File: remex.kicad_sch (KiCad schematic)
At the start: 8 parts

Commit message: added ADC circuits
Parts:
- added D? (x3): D_Zener, symbol Device:D_Zener
- added J?: ADC_B, symbol Connector:Screw_Terminal_01x03
- added J?: ADC_A, symbol Connector:Screw_Terminal_01x03
- added J? (x2): QEI, symbol Connector:Screw_Terminal_01x04
- added J?: ADC_C, symbol Connector:Screw_Terminal_01x03
- added R? (x6): R, symbol Device:R
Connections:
- net GND: now also D?.2 (A), D?.2 (A), D?.2 (A), J?.3 (Pin_3), J?.3 (Pin_3), J?.3 (Pin_3), R?.2, R?.2, R?.2
- net QEI circuit/GND: now also J?.1 (Pin_1)
- net QEI circuit/QEI_A_IN: now also J?.2 (Pin_2)
- net QEI circuit/QEI_B_IN: now also J?.3 (Pin_3)
- net QEI circuit/VBus: now also J?.4 (Pin_4)
- net QEI circuit1/GND: now also J?.1 (Pin_1)
- net QEI circuit1/QEI_A_IN: now also J?.2 (Pin_2)
- net QEI circuit1/QEI_B_IN: now also J?.3 (Pin_3)
- net QEI circuit1/VBus: now also J?.4 (Pin_4)
- net at U?.2 (P1.1): now also D?.1 (K), R?.1, R?.2
- net at U?.3 (P1.0): now also D?.1 (K), R?.1, R?.2
- net at U?.40 (P5.3): now also D?.1 (K), R?.1, R?.2
- new net: J?.1 (Pin_1), R?.1 (x3)

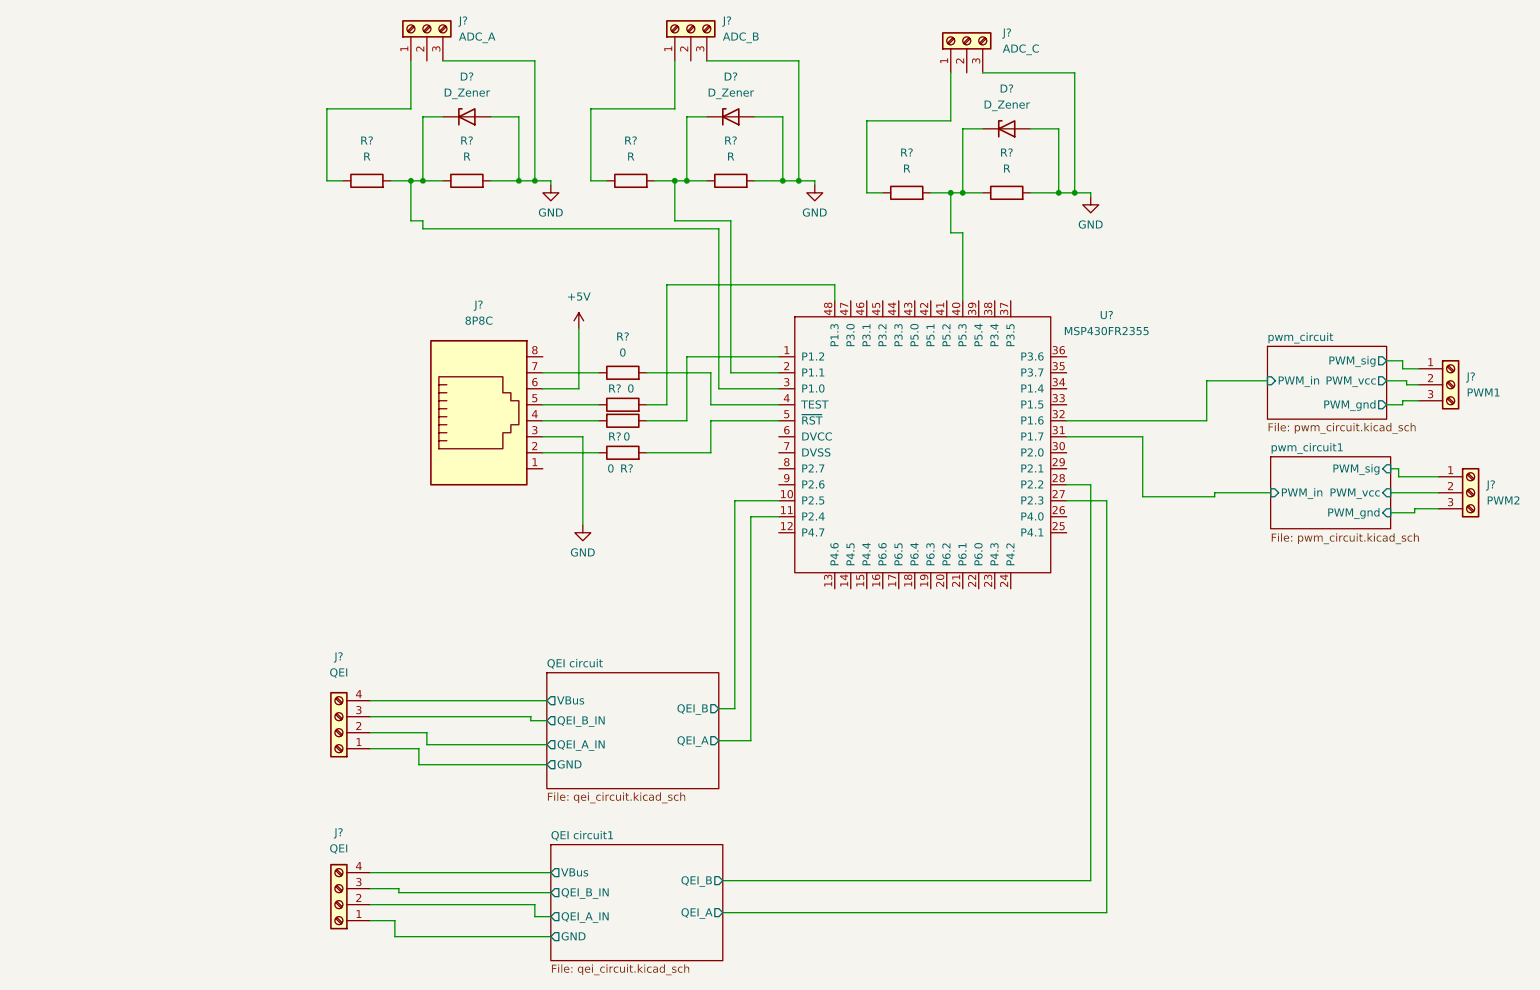
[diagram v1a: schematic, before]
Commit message: added foot prints
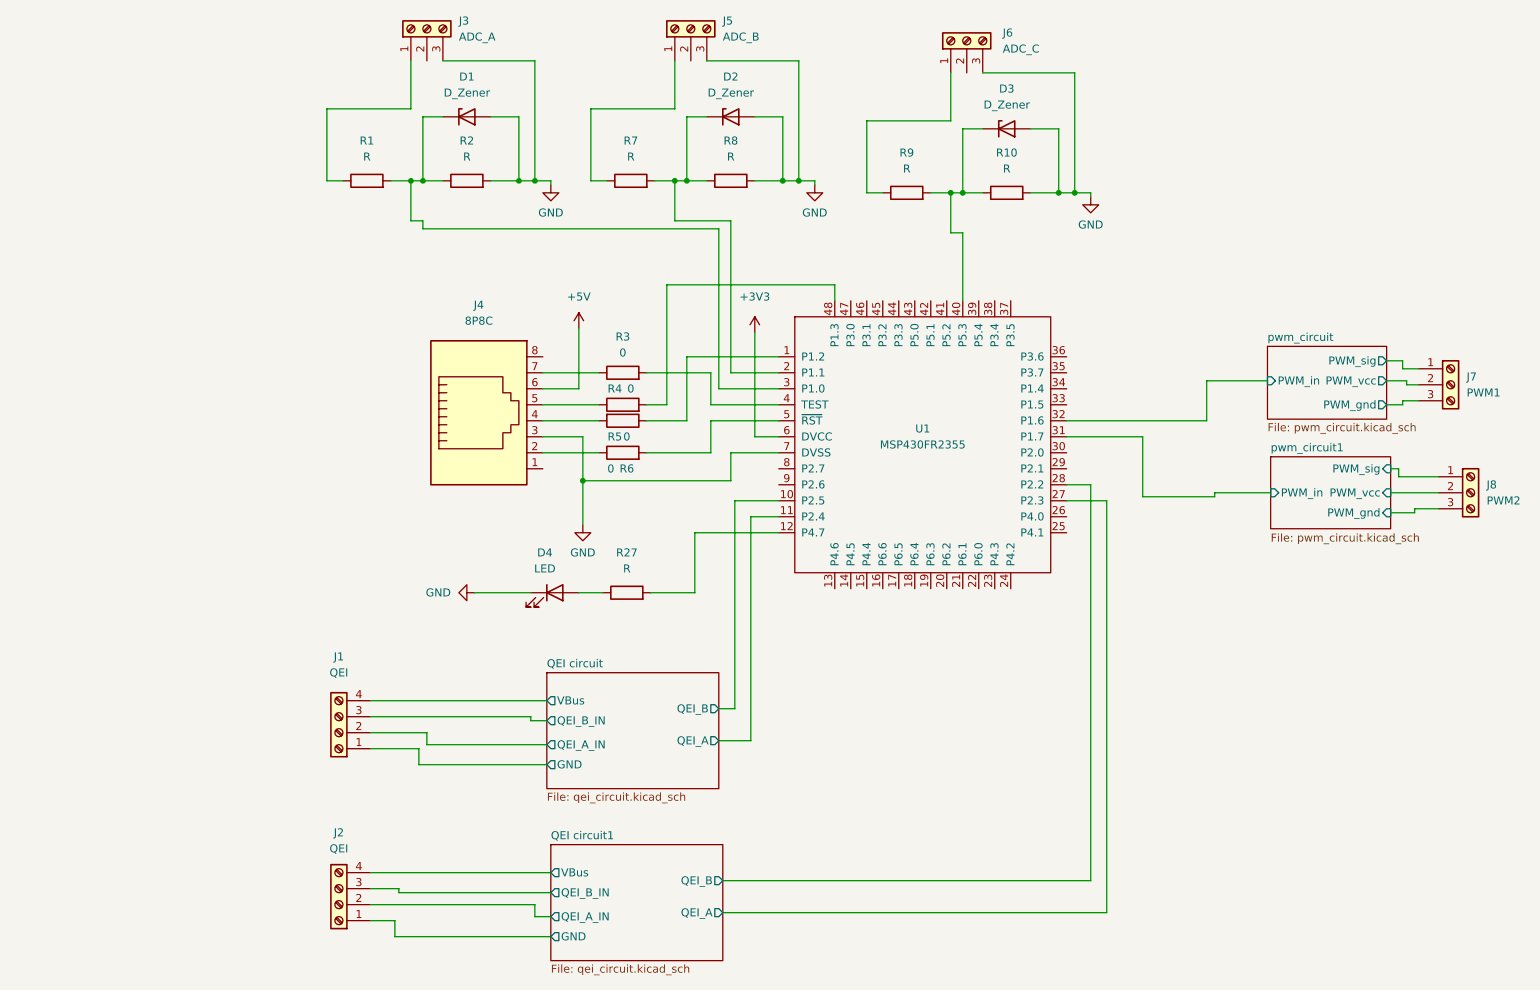
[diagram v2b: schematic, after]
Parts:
- added D4: LED, symbol Device:LED
- added R27: R, symbol Device:R
- D1, D2, D3: renamed from D?; footprint (none) -> Diode_SMD:D_0603_1608Metric
- J1, J2, J7: renamed from J?; footprint (none) -> TerminalBlock:TerminalBlock_bornier-4_P5.08mm
- J3, J5, J6, J8: renamed from J?; footprint (none) -> TerminalBlock:TerminalBlock_bornier-3_P5.08mm
- J4: renamed from J?; footprint (none) -> Connector_RJ:RJ45_Amphenol_54602-x08_Horizontal
- R1, R10, R2, R3, R4, R5, R6, R7, R8, R9: renamed from R?; footprint (none) -> Resistor_SMD:R_0603_1608Metric
- gave numbers to parts that had none: 1
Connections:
- net GND: now also U1.7 (DVSS), D4.1 (K)
- net at U1.12 (P4.7): now also R27.2
- net +3V3: now reaches U1.6 (DVCC)
- new net: D4.2 (A), R27.1

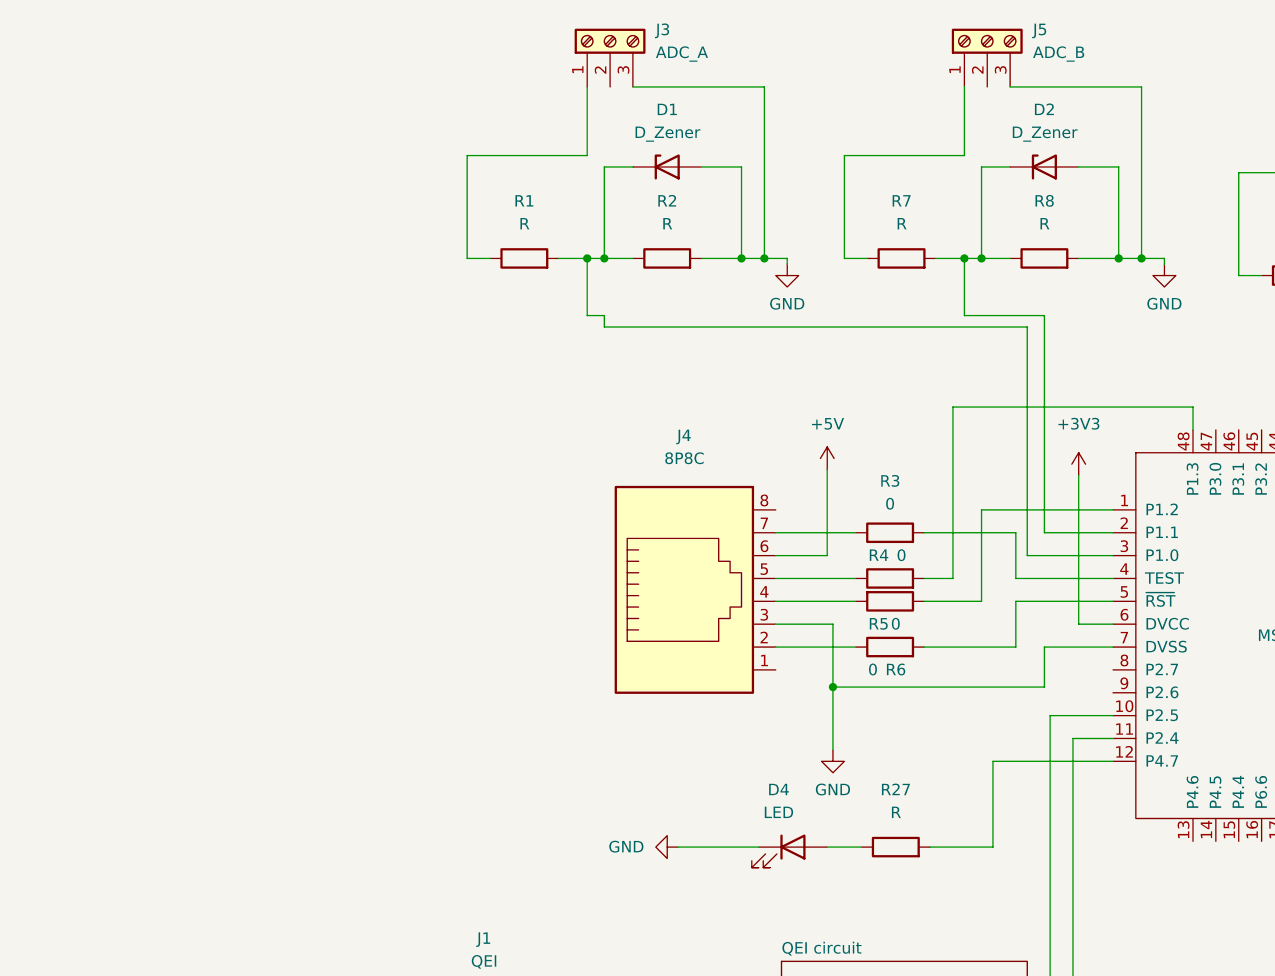
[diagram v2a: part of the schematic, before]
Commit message: added 3.3v regulator
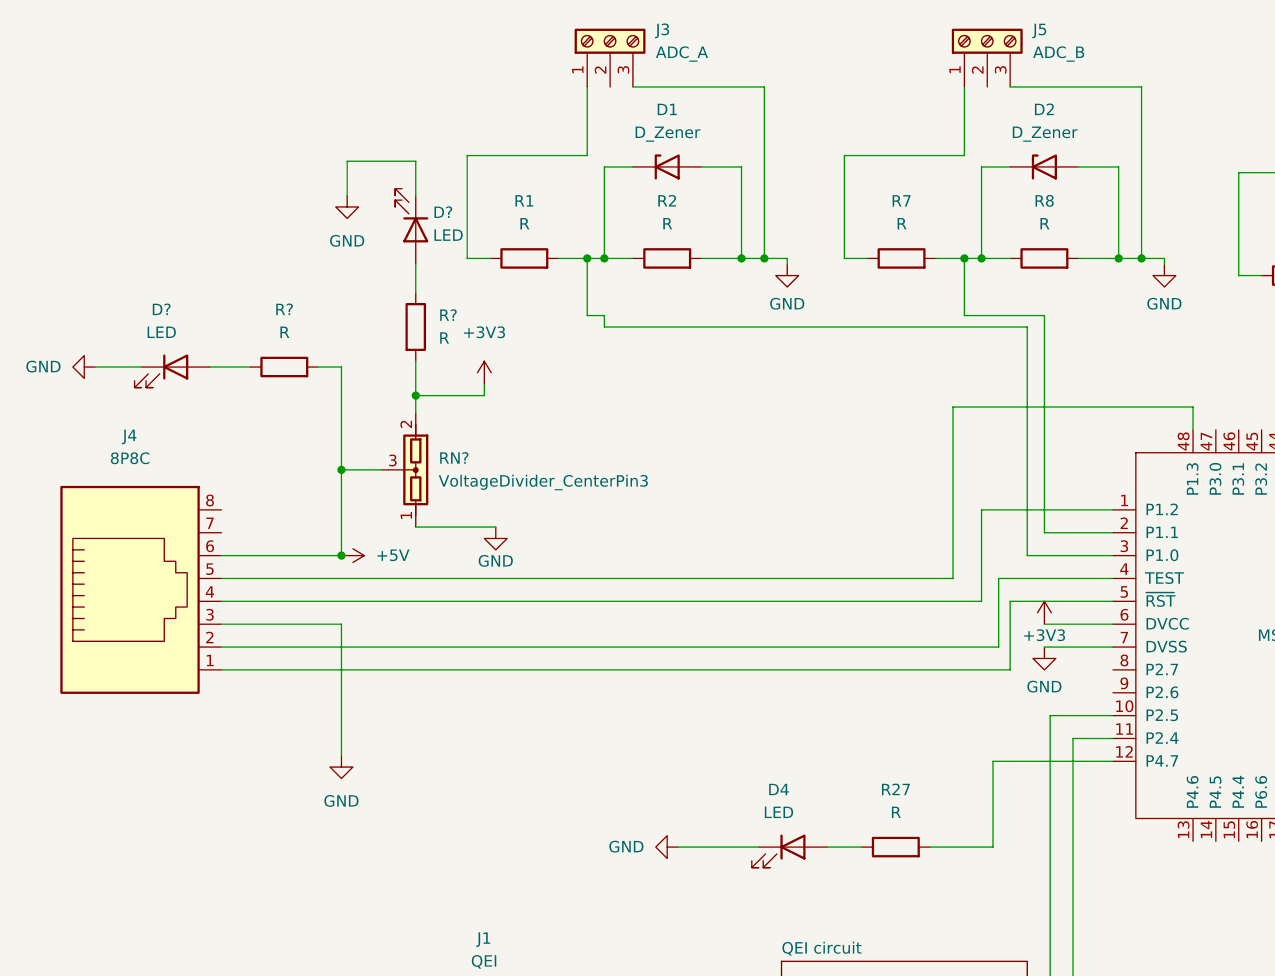
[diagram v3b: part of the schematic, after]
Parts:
- removed R3, R4, R5, R6: 0, Resistor_SMD:R_0603_1608Metric, symbol Device:R
- added D? (x2): LED, symbol Device:LED
- added R? (x2): R, symbol Device:R
- added RN?: VoltageDivider_CenterPin3, symbol Device:VoltageDivider_CenterPin3
- D4: footprint (none) -> LED_SMD:LED_0603_1608Metric
- R27: footprint (none) -> Resistor_SMD:R_0603_1608Metric
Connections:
- net +3V3: now also R?.2, RN?.2
- net +5V: now also R?.2, RN?.3
- net GND: now also D?.1 (K), D?.1 (K), RN?.1
- net at U1.4 (TEST): now also J4.2
- net at U1.1 (P1.2): now also J4.4
- net at U1.48 (P1.3): now also J4.5
- net at U1.5 (~{RST}): now also J4.1
- new net: D?.2 (A), R?.1 (x2)
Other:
- moved on the sheet: J4
